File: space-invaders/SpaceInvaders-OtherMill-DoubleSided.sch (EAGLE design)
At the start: 26 parts, among them J2-J4 TM4C123GXL, J3-J1 TM4C123GXL, J5 Nokia_5110, J6 Nokia_5110, J7 9V, U1 LM7805CT

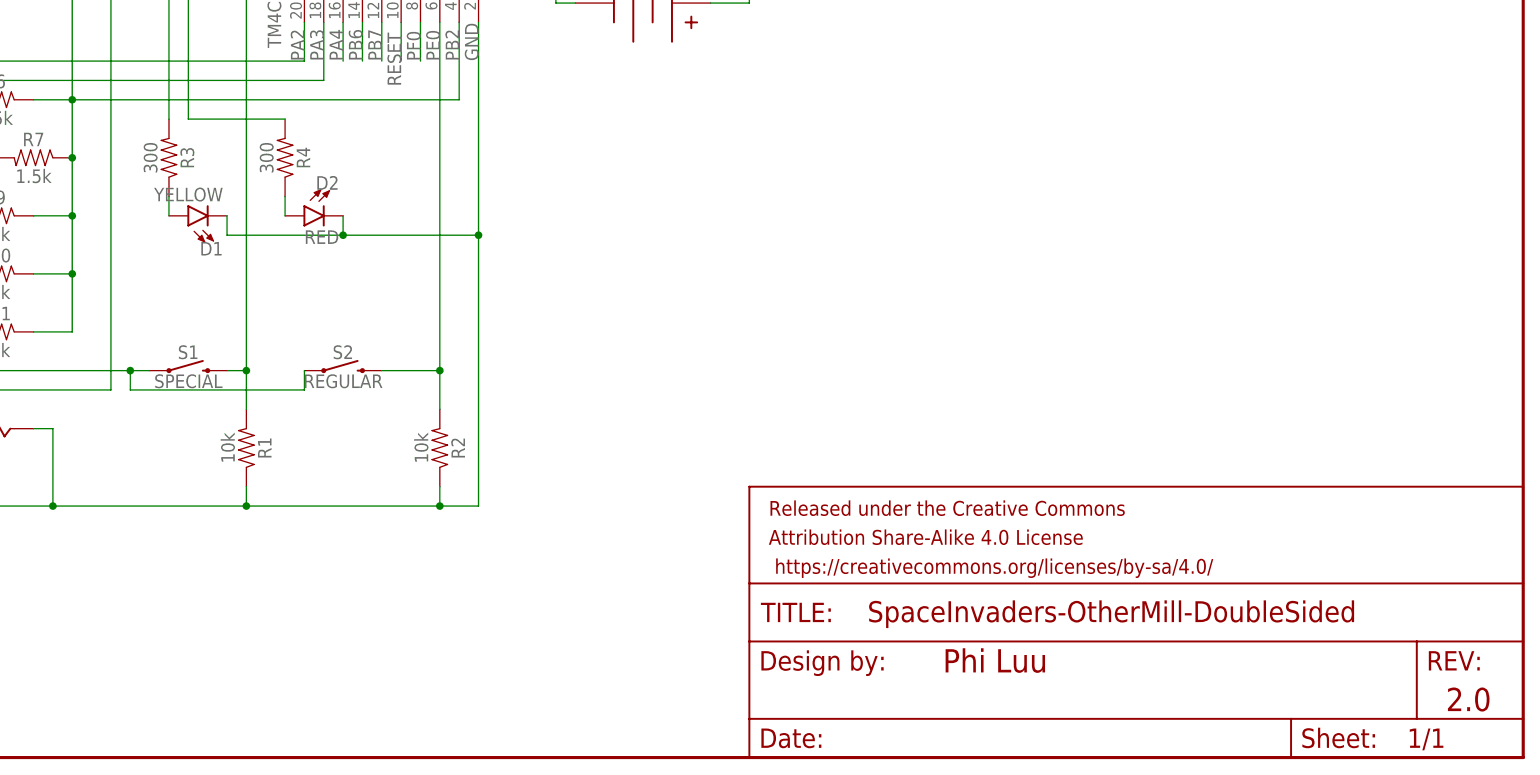
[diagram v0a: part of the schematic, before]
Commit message: Change LLED and RLED resistor value from 300 to 220
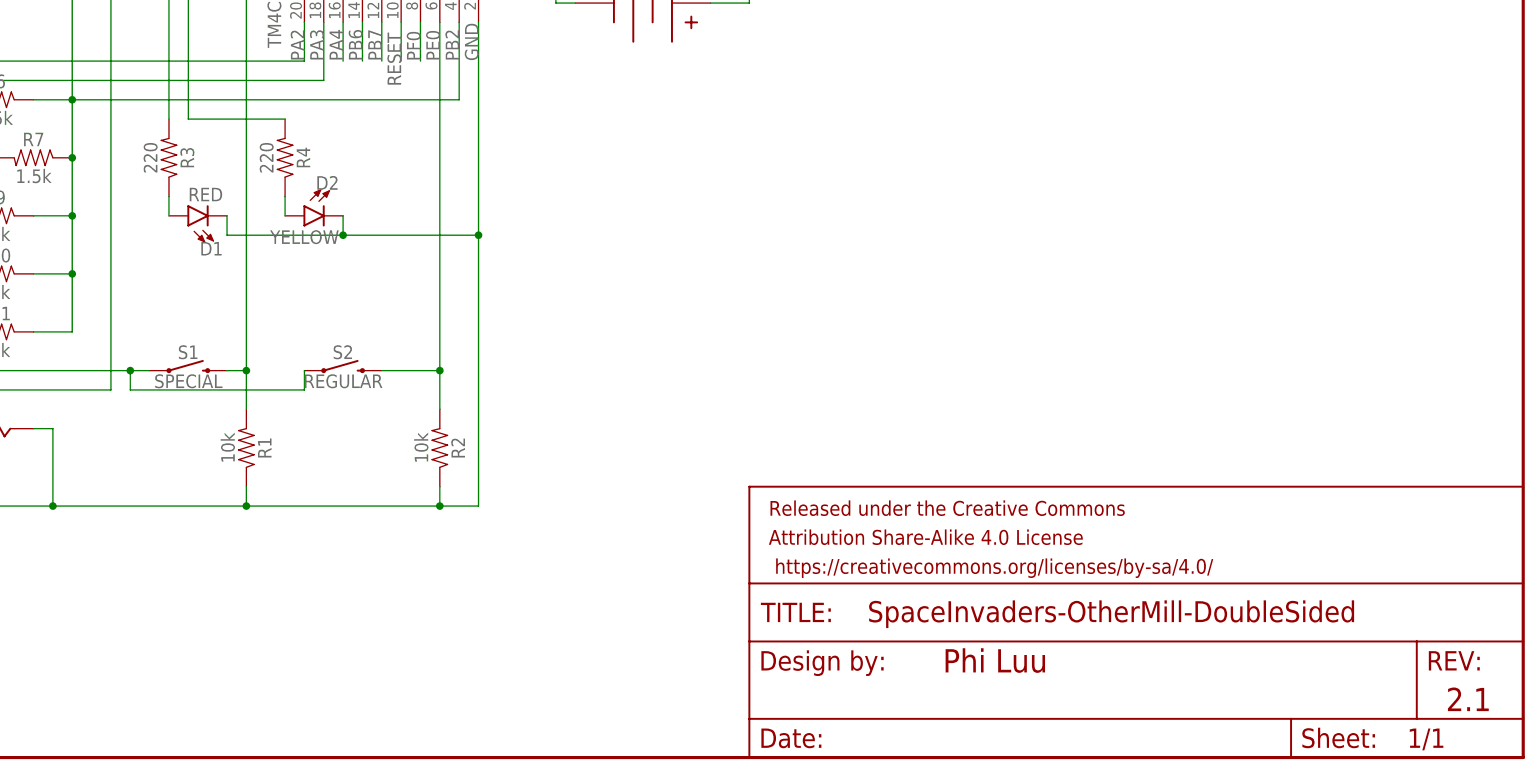
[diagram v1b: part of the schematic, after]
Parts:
- D1: value YELLOW -> RED
- D2: value RED -> YELLOW
- R3, R4: value 300 -> 220
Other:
- note added: "2.1"
- note removed: "2.0"
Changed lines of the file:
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@@
 <part name="LS1" library="SparkFun-Electromechanical" deviceset="BUZZER" device="-PTH" value="BUZZER"/>
 <part name="VR1" library="SparkFun-Resistors" deviceset="POTENTIOMETER_SLIDE" device="-30MM-1/10W-20%" value="10k"/>
-<part name="D1" library="SparkFun-LED" deviceset="LED" device="5MM" value="YELLOW"/>
-<part name="D2" library="SparkFun-LED" deviceset="LED" device="5MM" value="RED"/>
+<part name="D1" library="SparkFun-LED" deviceset="LED" device="5MM" value="RED"/>
+<part name="D2" library="SparkFun-LED" deviceset="LED" device="5MM" value="YELLOW"/>
 <part name="R1" library="SparkFun-Resistors" deviceset="10KOHM" device="-HORIZ-1/4W-5%" value="10k"/>
 <part name="R2" library="SparkFun-Resistors" deviceset="10KOHM" device="-HORIZ-1/4W-5%" value="10k"/>
-<part name="R3" library="SparkFun-Resistors" deviceset="1KOHM" device="-HORIZ-1/4W-5%" value="300"/>
-<part name="R4" library="SparkFun-Resistors" deviceset="1KOHM" device="-HORIZ-1/4W-5%" value="300"/>
+<part name="R3" library="SparkFun-Resistors" deviceset="1KOHM" device="-HORIZ-1/4W-5%" value="220"/>
+<part name="R4" library="SparkFun-Resistors" deviceset="1KOHM" device="-HORIZ-1/4W-5%" value="220"/>
 <part name="R5" library="SparkFun-Resistors" deviceset="1KOHM" device="-HORIZ-1/4W-5%" value="220"/>
 <part name="R6" library="SparkFun-Resistors" deviceset="1KOHM" device="-HORIZ-1/4W-5%" value="1.5k"/>
@@
 <plain>
 <text x="172.72" y="12.7" size="3.048" layer="94" font="vector" align="center-left">Phi Luu</text>
-<text x="238.76" y="7.62" size="3.048" layer="94" font="vector" align="center-left">2.0</text>
+<text x="238.76" y="7.62" size="3.048" layer="94" font="vector" align="center-left">2.1</text>
 <text x="106.68" y="148.844" size="1.778" layer="96" font="vector" rot="R90">PB0</text>
 <text x="104.14" y="148.844" size="1.778" layer="96" font="vector" rot="R90">PB1</text>

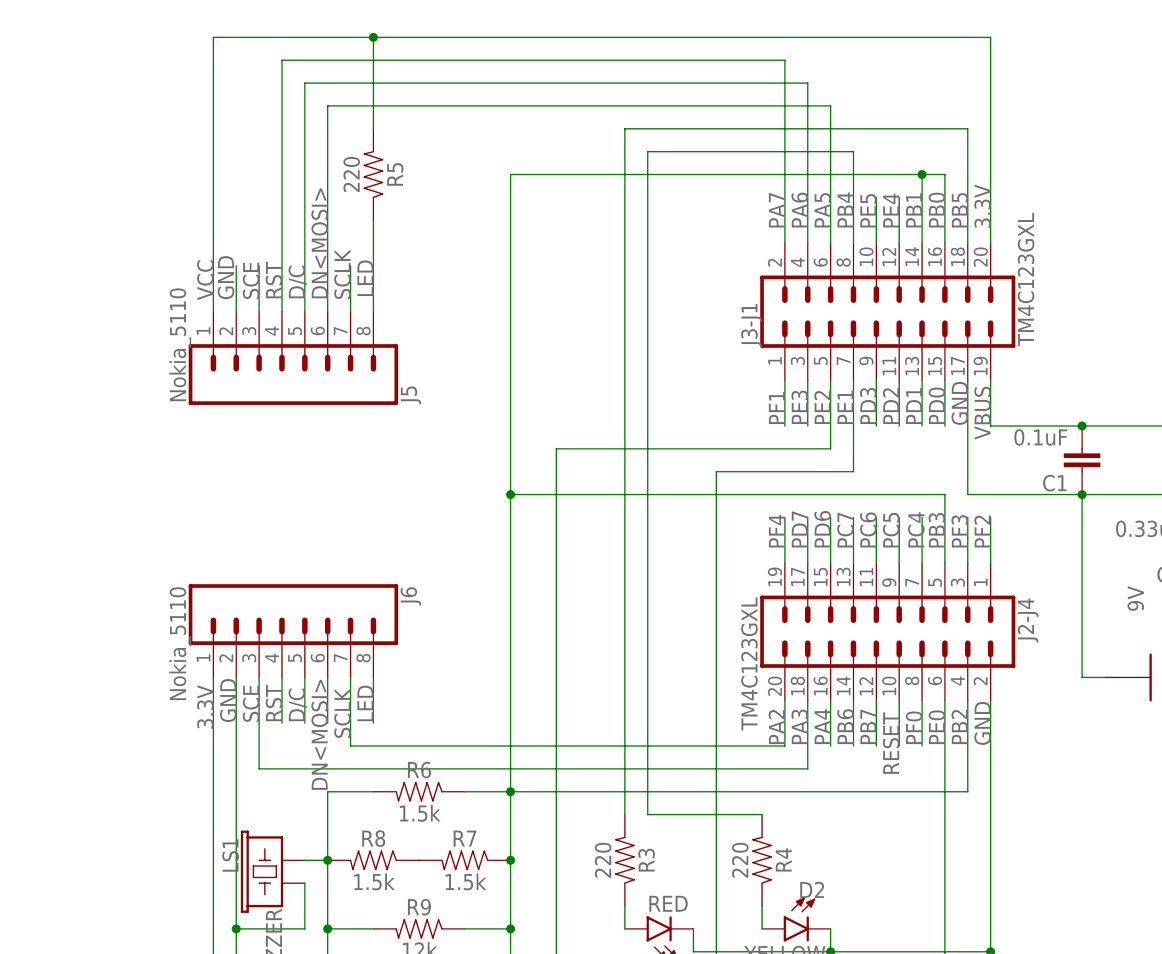
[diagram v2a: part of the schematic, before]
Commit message: Connect nets & Apply schematic convention
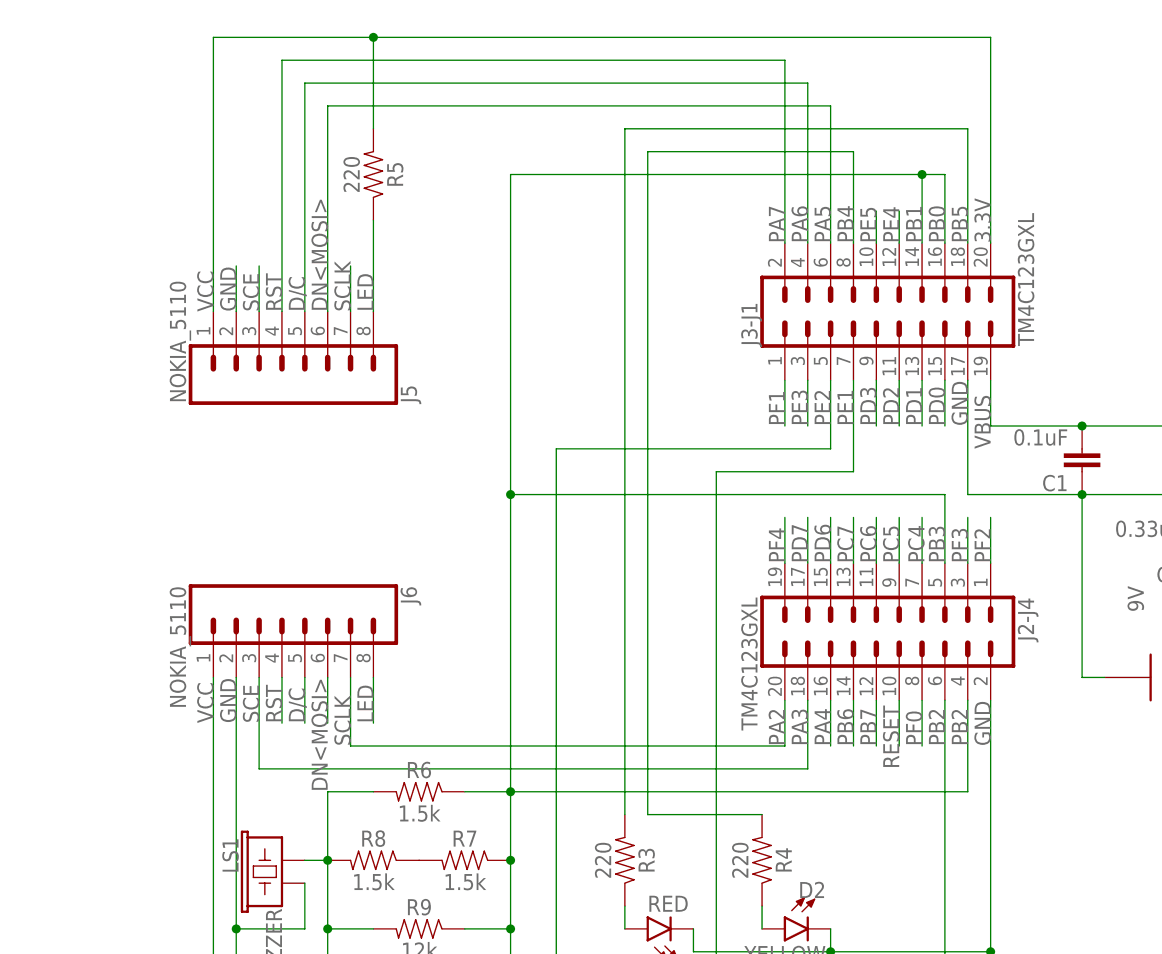
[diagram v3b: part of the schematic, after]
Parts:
- J5, J6: value Nokia_5110 -> NOKIA_5110
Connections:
- removed net D/C: J6.5
- removed net DN<MOSI>: J6.6
- removed net PE0: J2-J4.6, R2.2, S2.2
- removed net RST: J6.4
- removed net SCE: J5.3
- removed net SCLK: J5.7
- new net DAC: J2-J4.4, J2-J4.5, J3-J1.14, J3-J1.16, R10.1, R11.1, R6.1, R7.1, R9.1
- net PA2: now also J5.7
- net PA3: now also J5.3
- net PA5: now also J6.6
- net PA6: now also J6.5
- net PA7: now also J6.4
- net PB2: now also J2-J4.6, R2.2, S2.2; no longer J2-J4.4, J2-J4.5, J3-J1.14, J3-J1.16, R10.1, R11.1, R6.1, R7.1, R9.1

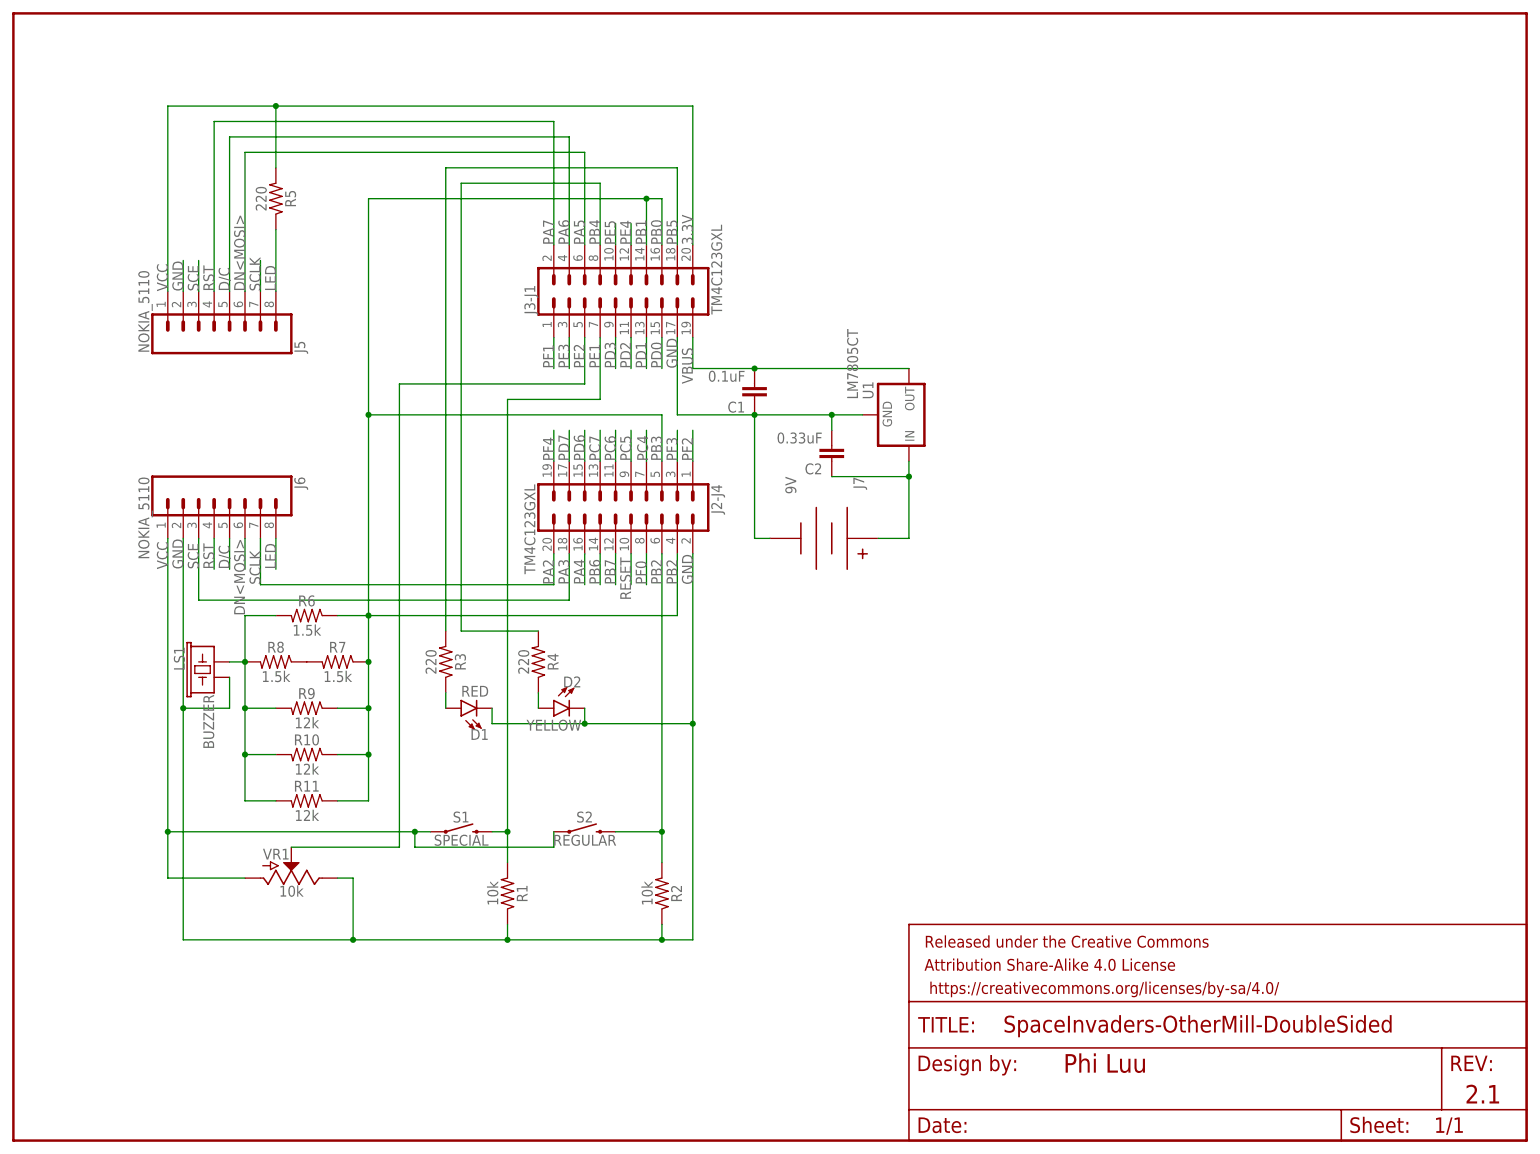
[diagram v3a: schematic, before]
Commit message: Expand & make more space in schematic
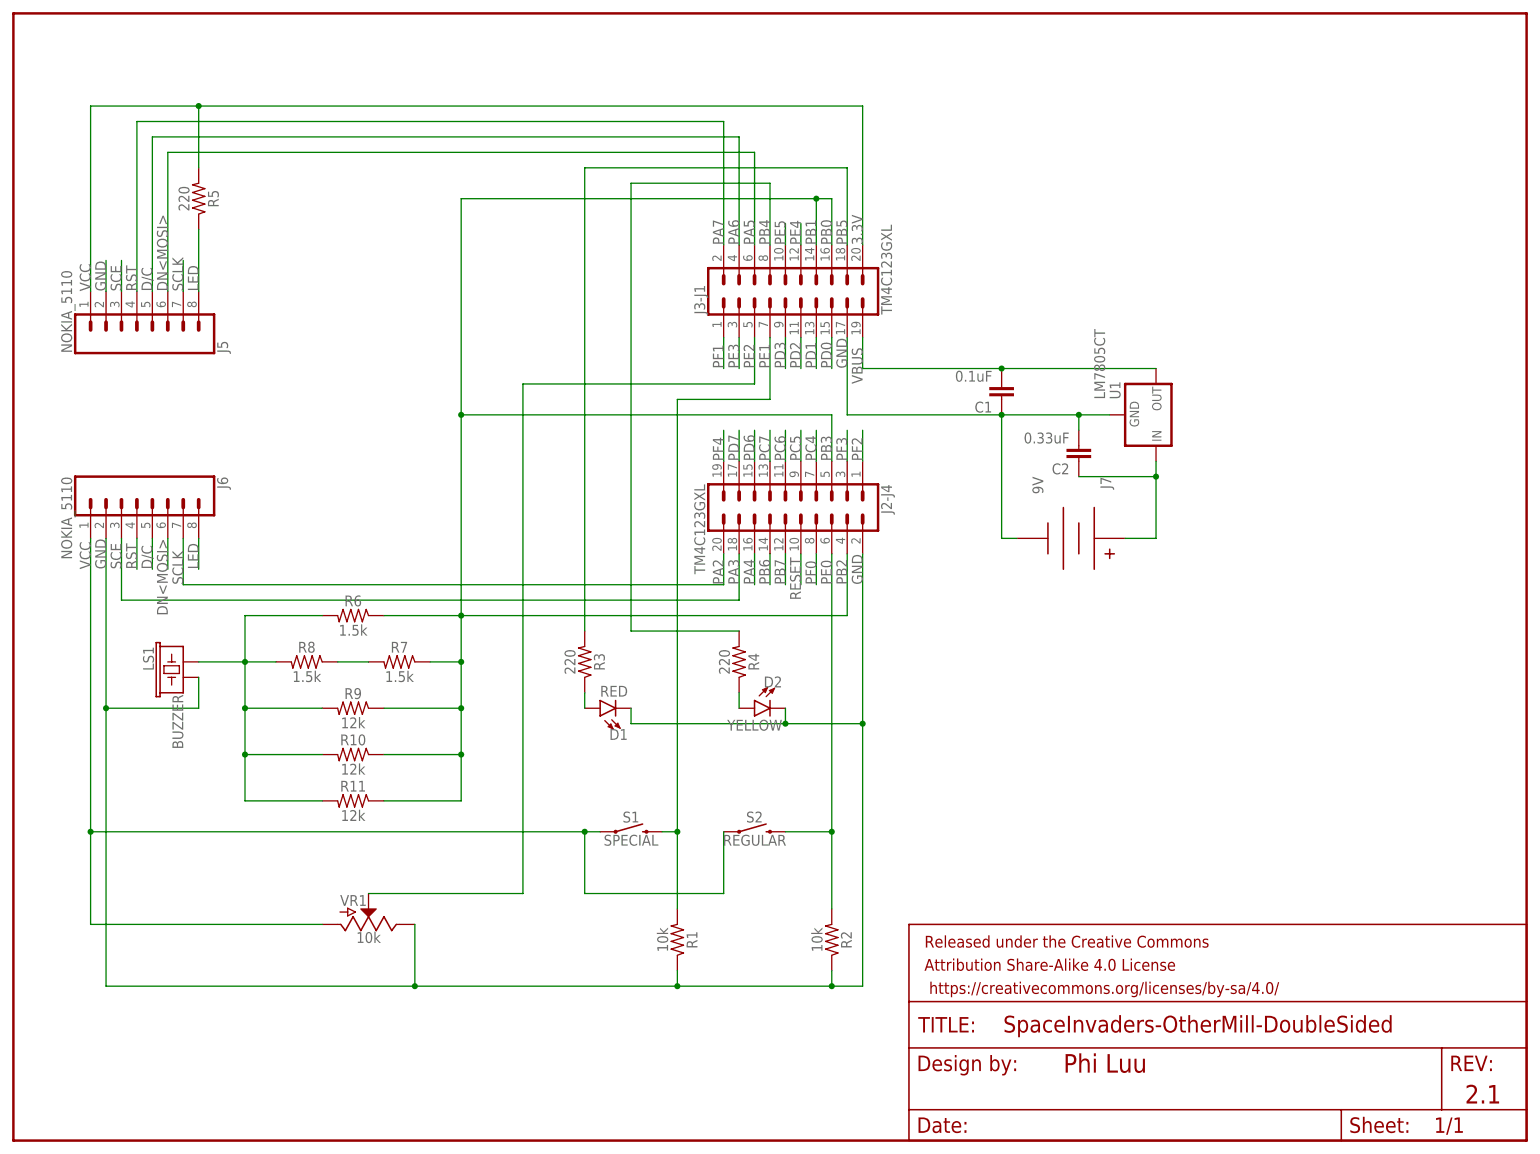
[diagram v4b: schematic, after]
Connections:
- net PB2 renamed PE0
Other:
- note added: "PB2"
- moved on the sheet: C1, C2, D1, D2, J2-J4, J3-J1, J5, J6, J7, LS1, R1, R10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
